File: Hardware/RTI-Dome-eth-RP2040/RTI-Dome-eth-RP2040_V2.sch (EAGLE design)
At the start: 106 parts, among them IC2 24LC64T-I/SN, IC3 FT232RL, IC4 RASPBERRY_PI_PICO, IC8 REG1117-3.3V, IC9 REG1117-5V, J2 XT60PW-M, T1 MMBT3904LT1, T2 MMBT3904LT1, T3 MMBT3904LT1, U1 W5500, X13 PN61729-S, X9 J1011F21PNL

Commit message: Soem minor fixes on the PCB
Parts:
- IC4: JLCPCBPN (none) -> C7203003
- X9: value J1011F21PNL -> J1011F01PNL; device rti:J1011F21PNL -> rti:J1011F01PNL; MPN J1011F21PNL -> (none)
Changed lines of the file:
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@@
 </classes>
 <parts>
-<part name="X4" library="rti" library_urn="urn:adsk.eagle:library:37256580" deviceset="AK500/3" device="" package3d_urn="urn:adsk.eagle:package:37500967/2">
+<part name="X4" library="rti" library_urn="urn:adsk.eagle:library:37256580" deviceset="AK500/3" device="" package3d_urn="urn:adsk.eagle:package:37500967/6">
 <attribute name="MPN" value="691101710003"/>
 </part>
-<part name="X1" library="rti" library_urn="urn:adsk.eagle:library:37256580" deviceset="AK500/2" device="" package3d_urn="urn:adsk.eagle:package:37318416/2">
+<part name="X1" library="rti" library_urn="urn:adsk.eagle:library:37256580" deviceset="AK500/2" device="" package3d_urn="urn:adsk.eagle:package:37318416/4">
 <attribute name="MPN" value="691101710002"/>
 </part>
-<part name="X3" library="rti" library_urn="urn:adsk.eagle:library:37256580" deviceset="AK500/2" device="" package3d_urn="urn:adsk.eagle:package:37318416/2">
+<part name="X3" library="rti" library_urn="urn:adsk.eagle:library:37256580" deviceset="AK500/2" device="" package3d_urn="urn:adsk.eagle:package:37318416/4">
 <attribute name="MPN" value="691101710002"/>
 </part>
-<part name="X5" library="rti" library_urn="urn:adsk.eagle:library:37256580" deviceset="AK500/3" device="" package3d_urn="urn:adsk.eagle:package:37500967/2">
+<part name="X5" library="rti" library_urn="urn:adsk.eagle:library:37256580" deviceset="AK500/3" device="" package3d_urn="urn:adsk.eagle:package:37500967/6">
 <attribute name="MPN" value="691101710003"/>
 </part>
@@
 <attribute name="MPN" value="CC0805KKX5R8BB106"/>
 </part>
-<part name="X8" library="rti" library_urn="urn:adsk.eagle:library:37256580" deviceset="AK500/2" device="" package3d_urn="urn:adsk.eagle:package:37318416/2">
+<part name="X8" library="rti" library_urn="urn:adsk.eagle:library:37256580" deviceset="AK500/2" device="" package3d_urn="urn:adsk.eagle:package:37318416/4">
 <attribute name="MPN" value="691101710002"/>
 </part>
-<part name="X11" library="rti" library_urn="urn:adsk.eagle:library:37256580" deviceset="AK500/2" device="" package3d_urn="urn:adsk.eagle:package:37318416/2">
+<part name="X11" library="rti" library_urn="urn:adsk.eagle:library:37256580" deviceset="AK500/2" device="" package3d_urn="urn:adsk.eagle:package:37318416/4">
 <attribute name="MPN" value="691101710002"/>
 </part>
@@
 <attribute name="MPN" value="RC0805FR-0749R9L"/>
 </part>
-<part name="X9" library="rti" library_urn="urn:adsk.eagle:library:37256580" deviceset="J1011F" device="" package3d_urn="urn:adsk.eagle:package:37318428/2" technology="21PNL" value="J1011F21PNL">
-<attribute name="MPN" value="J1011F21PNL"/>
-</part>
+<part name="X9" library="rti" library_urn="urn:adsk.eagle:library:37256580" deviceset="J1011F01PNL" device="" package3d_urn="urn:adsk.eagle:package:43182963/4" value="J1011F01PNL"/>
 <part name="R31" library="rcl" library_urn="urn:adsk.eagle:library:334" deviceset="R-EU_" device="R0603" package3d_urn="urn:adsk.eagle:package:23555/3" value="4.7K">
 <spice>
@@
 <part name="GND16" library="supply1" library_urn="urn:adsk.eagle:library:371" deviceset="GND" device=""/>
 <part name="J2" library="samacsys" library_urn="urn:adsk.eagle:library:37256869" deviceset="XT60PW-M" device="" package3d_urn="urn:adsk.eagle:package:37256940/5"/>
-<part name="X2" library="rti" library_urn="urn:adsk.eagle:library:37256580" deviceset="AK500/3" device="" package3d_urn="urn:adsk.eagle:package:37500967/2"/>
-<part name="X10" library="rti" library_urn="urn:adsk.eagle:library:37256580" deviceset="AK500/3" device="" package3d_urn="urn:adsk.eagle:package:37500967/2"/>
+<part name="X2" library="rti" library_urn="urn:adsk.eagle:library:37256580" deviceset="AK500/3" device="" package3d_urn="urn:adsk.eagle:package:37500967/6"/>
+<part name="X10" library="rti" library_urn="urn:adsk.eagle:library:37256580" deviceset="AK500/3" device="" package3d_urn="urn:adsk.eagle:package:37500967/6"/>
 <part name="IC2" library="Microchip_By_element14_Batch_1" deviceset="24LC64T-I/SN" device=""/>
 <part name="GND21" library="supply1" library_urn="urn:adsk.eagle:library:371" deviceset="GND" device=""/>
@@
 </part>
 <part name="GND38" library="supply1" library_urn="urn:adsk.eagle:library:371" deviceset="GND" device=""/>
-<part name="IC4" library="samacsys" library_urn="urn:adsk.eagle:library:37256869" deviceset="RASPBERRY_PI_PICO" device="" package3d_urn="urn:adsk.eagle:package:40546189/5" value="RASPBERRY_PI_PICO">
+<part name="IC4" library="samacsys" library_urn="urn:adsk.eagle:library:37256869" deviceset="RASPBERRY_PI_PICO" device="" package3d_urn="urn:adsk.eagle:package:40546189/7" value="RASPBERRY_PI_PICO">
 <attribute name="DESCRIPTION" value="RASPBERRY-PI - RASPBERRY PI PICO - Raspberry Pi Board, Raspberry Pi Pic, RP2040, 32bit, ARM Cortex-M0+"/>
+<attribute name="JLCPCBPN" value="C7203003"/>
 <attribute name="MANUFACTURER_NAME" value="RASPBERRY-PI PICO"/>
 <attribute name="MANUFACTURER_PART_NUMBER" value="SC0916"/>
@@
 <attribute name="MPN" value="SS-52300-001"/>
 </part>
-<part name="X6" library="rti" library_urn="urn:adsk.eagle:library:37256580" deviceset="AK500/3" device="" package3d_urn="urn:adsk.eagle:package:37500967/2"/>
-<part name="X12" library="rti" library_urn="urn:adsk.eagle:library:37256580" deviceset="AK500/2" device="" package3d_urn="urn:adsk.eagle:package:37318416/2">
+<part name="X6" library="rti" library_urn="urn:adsk.eagle:library:37256580" deviceset="AK500/3" device="" package3d_urn="urn:adsk.eagle:package:37500967/6"/>
+<part name="X12" library="rti" library_urn="urn:adsk.eagle:library:37256580" deviceset="AK500/2" device="" package3d_urn="urn:adsk.eagle:package:37318416/4">
 <attribute name="MPN" value="691101710002"/>
 </part>
@@
 <attribute name="VALUE" x="83.82" y="66.04" size="1.778" layer="96" align="center-left"/>
 <attribute name="MPN" x="109.22" y="40.64" size="1.778" layer="96" display="off"/>
+<attribute name="JLCPCBPN" x="109.22" y="40.64" size="1.778" layer="96" display="off"/>
 </instance>
 <instance part="X13" gate="G$1" x="335.28" y="180.34" smashed="yes" rot="R180">

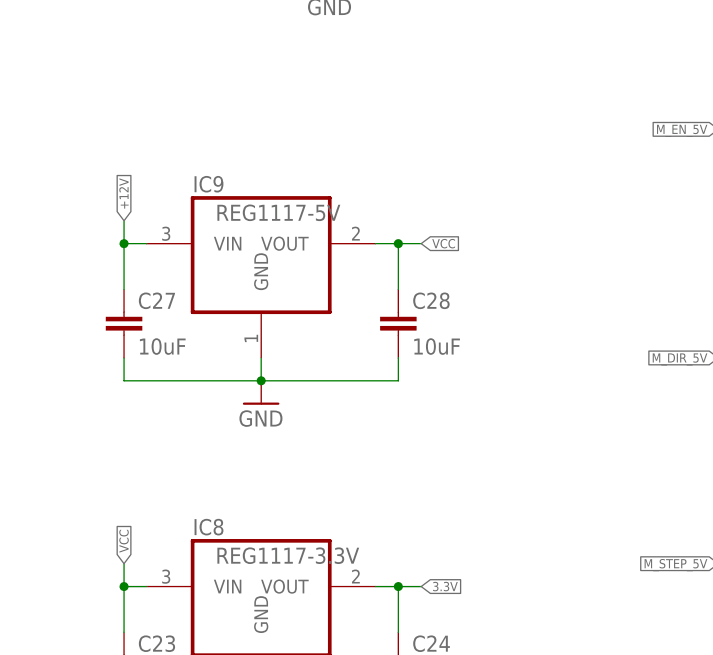
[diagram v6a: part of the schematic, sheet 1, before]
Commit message: Change 5V regulator for 1A version
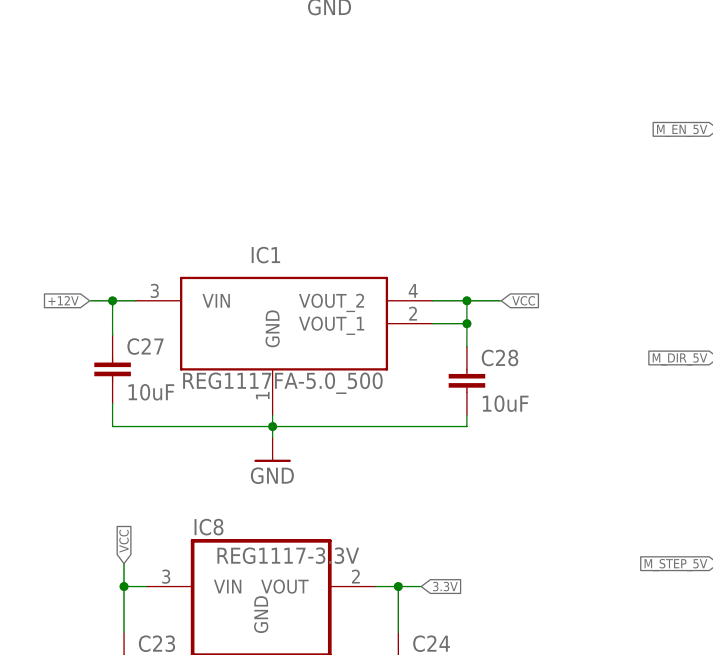
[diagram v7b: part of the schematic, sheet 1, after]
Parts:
- removed IC9: REG1117-5V, burr-brown:REG1117
- added IC1: REG1117FA-5.0_500, REG1117FA-5.0_500:REG1117FA-5.0_500
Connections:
- net +12V: now also IC1.VIN; no longer IC9.VIN
- net GND: now also IC1.GND; no longer IC9.GND
- net VCC: now also IC1.VOUT_1, IC1.VOUT_2; no longer IC9.VOUT
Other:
- moved on the sheet: C27, C28
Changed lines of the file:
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@@
 </part>
 <part name="GND22" library="supply1" library_urn="urn:adsk.eagle:library:371" deviceset="GND" device=""/>
-<part name="IC9" library="burr-brown" library_urn="urn:adsk.eagle:library:37504555" deviceset="REG1117" device="" package3d_urn="urn:adsk.eagle:package:37504714/1" value="REG1117-5V">
-<attribute name="MPN" value="REG1117-3.3/2K5"/>
-</part>
 <part name="C27" library="rcl" library_urn="urn:adsk.eagle:library:334" deviceset="C-EU" device="C0603" package3d_urn="urn:adsk.eagle:package:23616/2" value="10uF">
 <spice>
@@
 <attribute name="MPN" value="CC0805KKX5R8BB106"/>
 </part>
-<part name="GND23" library="supply1" library_urn="urn:adsk.eagle:library:371" deviceset="GND" device=""/>
 <part name="R9" library="rcl" library_urn="urn:adsk.eagle:library:334" deviceset="R-EU_" device="R0603" package3d_urn="urn:adsk.eagle:package:23555/3" value="4.7K">
 <spice>
@@
 <attribute name="MPN" value="RT0805FRE074K7L"/>
 </part>
+<part name="IC1" library="REG1117FA-5.0_500" library_urn="urn:adsk.eagle:library:43937876" deviceset="REG1117FA-5.0_500" device="" package3d_urn="urn:adsk.eagle:package:43937879/3"/>
+<part name="GND3" library="supply1" library_urn="urn:adsk.eagle:library:371" deviceset="GND" device=""/>
 </parts>
 <sheets>
@@
 <attribute name="VALUE" x="27.94" y="93.98" size="1.778" layer="96"/>
 </instance>
-<instance part="IC9" gate="G$1" x="30.48" y="152.4" smashed="yes">
-<attribute name="NAME" x="22.86" y="158.115" size="1.778" layer="95" ratio="10"/>
-<attribute name="VALUE" x="25.4" y="154.94" size="1.778" layer="96" ratio="10"/>
-</instance>
-<instance part="C27" gate="G$1" x="15.24" y="144.78" smashed="yes">
-<attribute name="MPN" x="15.24" y="144.78" size="1.778" layer="96" display="off"/>
-<attribute name="NAME" x="16.764" y="145.161" size="1.778" layer="95"/>
-<attribute name="VALUE" x="16.764" y="140.081" size="1.778" layer="96"/>
-</instance>
-<instance part="C28" gate="G$1" x="45.72" y="144.78" smashed="yes">
-<attribute name="MPN" x="45.72" y="144.78" size="1.778" layer="96" display="off"/>
-<attribute name="NAME" x="47.244" y="145.161" size="1.778" layer="95"/>
-<attribute name="VALUE" x="47.244" y="140.081" size="1.778" layer="96"/>
-</instance>
-<instance part="GND23" gate="1" x="30.48" y="134.62" smashed="yes">
-<attribute name="VALUE" x="27.94" y="132.08" size="1.778" layer="96"/>
+<instance part="C27" gate="G$1" x="13.97" y="139.7" smashed="yes">
+<attribute name="MPN" x="13.97" y="139.7" size="1.778" layer="96" display="off"/>
+<attribute name="NAME" x="15.494" y="140.081" size="1.778" layer="95"/>
+<attribute name="VALUE" x="15.494" y="135.001" size="1.778" layer="96"/>
+</instance>
+<instance part="C28" gate="G$1" x="53.34" y="138.43" smashed="yes">
+<attribute name="MPN" x="53.34" y="138.43" size="1.778" layer="96" display="off"/>
+<attribute name="NAME" x="54.864" y="138.811" size="1.778" layer="95"/>
+<attribute name="VALUE" x="54.864" y="133.731" size="1.778" layer="96"/>
 </instance>
 <instance part="R9" gate="G$1" x="285.75" y="241.3" smashed="yes" rot="R270">
@@
 <attribute name="NAME" x="92.71" y="115.3414" size="1.778" layer="95" rot="R180"/>
 <attribute name="VALUE" x="92.71" y="120.142" size="1.778" layer="96" rot="R180"/>
+</instance>
+<instance part="IC1" gate="G$1" x="16.51" y="146.05" smashed="yes">
+<attribute name="NAME" x="29.21" y="151.13" size="1.778" layer="95" align="center-left"/>
+<attribute name="VALUE" x="21.59" y="137.16" size="1.778" layer="96" align="center-left"/>
+</instance>
+<instance part="GND3" gate="1" x="31.75" y="128.27" smashed="yes">
+<attribute name="VALUE" x="29.21" y="125.73" size="1.778" layer="96"/>
 </instance>
 </instances>
@@
 </segment>
 <segment>
-<pinref part="IC9" gate="G$1" pin="GND"/>
-<wire x1="30.48" y1="137.16" x2="30.48" y2="139.7" width="0.1524" layer="91"/>
-<pinref part="C28" gate="G$1" pin="2"/>
-<wire x1="45.72" y1="139.7" x2="45.72" y2="137.16" width="0.1524" layer="91"/>
-<wire x1="45.72" y1="137.16" x2="30.48" y2="137.16" width="0.1524" layer="91"/>
-<junction x="30.48" y="137.16"/>
-<pinref part="C27" gate="G$1" pin="2"/>
-<wire x1="15.24" y1="139.7" x2="15.24" y2="137.16" width="0.1524" layer="91"/>
-<wire x1="15.24" y1="137.16" x2="30.48" y2="137.16" width="0.1524" layer="91"/>
-<pinref part="GND23" gate="1" pin="GND"/>
-</segment>
-<segment>
 <pinref part="GND32" gate="1" pin="GND"/>
 <pinref part="C40" gate="G$1" pin="2"/>
@@
 <pinref part="U$1" gate="G$1" pin="A3"/>
 </segment>
+<segment>
+<pinref part="IC1" gate="G$1" pin="GND"/>
+<wire x1="31.75" y1="130.81" x2="31.75" y2="132.08" width="0.1524" layer="91"/>
+<pinref part="GND3" gate="1" pin="GND"/>
+<pinref part="C27" gate="G$1" pin="2"/>
+<wire x1="31.75" y1="132.08" x2="31.75" y2="133.35" width="0.1524" layer="91"/>
+<wire x1="13.97" y1="134.62" x2="13.97" y2="132.08" width="0.1524" layer="91"/>
+<wire x1="13.97" y1="132.08" x2="31.75" y2="132.08" width="0.1524" layer="91"/>
+<junction x="31.75" y="132.08"/>
+<pinref part="C28" gate="G$1" pin="2"/>
+<wire x1="31.75" y1="132.08" x2="53.34" y2="132.08" width="0.1524" layer="91"/>
+<wire x1="53.34" y1="132.08" x2="53.34" y2="133.35" width="0.1524" layer="91"/>
+</segment>
 </net>
 <net name="+12V" class="1">
@@
 </segment>
 <segment>
+<pinref part="IC1" gate="G$1" pin="VIN"/>
+<wire x1="11.43" y1="146.05" x2="13.97" y2="146.05" width="0.1524" layer="91"/>
+<label x="11.43" y="146.05" size="1.016" layer="95" rot="R180" xref="yes"/>
+<wire x1="13.97" y1="146.05" x2="16.51" y2="146.05" width="0.1524" layer="91"/>
+<wire x1="13.97" y1="146.05" x2="13.97" y2="142.24" width="0.1524" layer="91"/>
+<junction x="13.97" y="146.05"/>
 <pinref part="C27" gate="G$1" pin="1"/>
-<pinref part="IC9" gate="G$1" pin="VIN"/>
-<wire x1="15.24" y1="147.32" x2="15.24" y2="152.4" width="0.1524" layer="91"/>
-<wire x1="15.24" y1="152.4" x2="17.78" y2="152.4" width="0.1524" layer="91"/>
-<wire x1="15.24" y1="154.94" x2="15.24" y2="152.4" width="0.1524" layer="91"/>
-<junction x="15.24" y="152.4"/>
-<label x="15.24" y="154.94" size="1.016" layer="95" rot="R90" xref="yes"/>
 </segment>
 </net>
@@
 </segment>
 <segment>
-<pinref part="IC9" gate="G$1" pin="VOUT"/>
-<pinref part="C28" gate="G$1" pin="1"/>
-<wire x1="43.18" y1="152.4" x2="45.72" y2="152.4" width="0.1524" layer="91"/>
-<wire x1="45.72" y1="152.4" x2="45.72" y2="147.32" width="0.1524" layer="91"/>
-<wire x1="48.26" y1="152.4" x2="45.72" y2="152.4" width="0.1524" layer="91"/>
-<junction x="45.72" y="152.4"/>
-<label x="48.26" y="152.4" size="1.016" layer="95" ratio="4" xref="yes"/>
-</segment>
-<segment>
 <pinref part="IC4" gate="G$1" pin="VSYS"/>
 <wire x1="161.29" y1="58.42" x2="158.75" y2="58.42" width="0.1524" layer="91"/>
@@
 <label x="106.68" y="124.46" size="1.016" layer="95" rot="R90" xref="yes"/>
 </segment>
-</net>
+<segment>
+<pinref part="IC1" gate="G$1" pin="VOUT_2"/>
+<wire x1="49.53" y1="146.05" x2="53.34" y2="146.05" width="0.1524" layer="91"/>
+<pinref part="IC1" gate="G$1" pin="VOUT_1"/>
+<wire x1="53.34" y1="146.05" x2="57.15" y2="146.05" width="0.1524" layer="91"/>
+<wire x1="49.53" y1="143.51" x2="53.34" y2="143.51" width="0.1524" layer="91"/>
+<wire x1="53.34" y1="143.51" x2="53.34" y2="146.05" width="0.1524" layer="91"/>
+<junction x="53.34" y="146.05"/>
+<label x="57.15" y="146.05" size="1.016" layer="95" xref="yes"/>
+<wire x1="53.34" y1="143.51" x2="53.34" y2="140.97" width="0.1524" layer="91"/>
+<junction x="53.34" y="143.51"/>
+<pinref part="C28" gate="G$1" pin="1"/>
+</segment>
+</net>

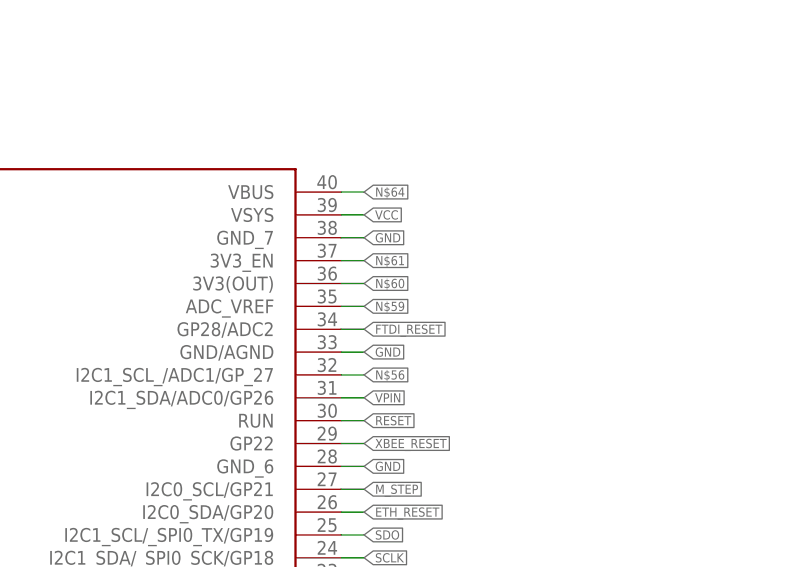
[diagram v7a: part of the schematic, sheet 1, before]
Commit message: Adding the same code for the RP2040 but using the lwIP_w5500 lib.
This is still not 100% functional as the same code is 25 times
slower to respond to queries. Next step is to wire the INT pin
on the PCB to try to address this issue.
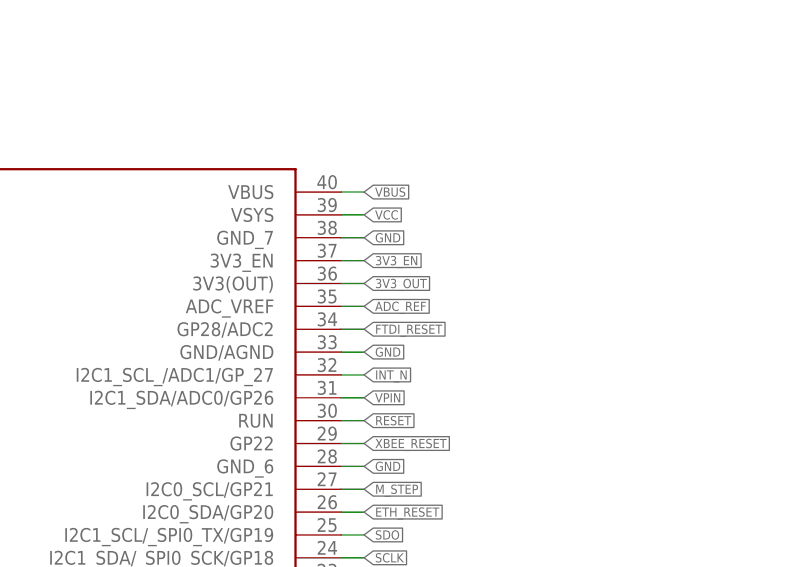
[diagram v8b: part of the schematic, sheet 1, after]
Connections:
- net N$59 renamed ADC_REF
- net N$60 renamed 3V3_OUT
- net N$61 renamed 3V3_EN
- net N$64 renamed VBUS
- removed net N$56: IC4.I2C1_SCL_/ADC1/GP_27
- net INT_N: now also IC4.I2C1_SCL_/ADC1/GP_27
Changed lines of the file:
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@@
 </segment>
 </net>
-<net name="N$56" class="0">
+<net name="INT_N" class="0">
 <segment>
 <pinref part="IC4" gate="G$1" pin="I2C1_SCL_/ADC1/GP_27"/>
@@
 </segment>
 </net>
-<net name="N$59" class="0">
+<net name="ADC_REF" class="0">
 <segment>
 <pinref part="IC4" gate="G$1" pin="ADC_VREF"/>
@@
 </segment>
 </net>
-<net name="N$60" class="0">
+<net name="3V3_OUT" class="0">
 <segment>
 <pinref part="IC4" gate="G$1" pin="3V3(OUT)"/>
@@
 </segment>
 </net>
-<net name="N$61" class="0">
+<net name="3V3_EN" class="0">
 <segment>
 <pinref part="IC4" gate="G$1" pin="3V3_EN"/>
@@
 </segment>
 </net>
-<net name="N$64" class="0">
+<net name="VBUS" class="0">
 <segment>
 <pinref part="IC4" gate="G$1" pin="VBUS"/>
